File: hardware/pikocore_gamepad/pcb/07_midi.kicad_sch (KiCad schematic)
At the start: 10 parts, among them J6 MIDI IN, J7 MIDI OUT, U10 H11L1M, U9 74LVC1G17

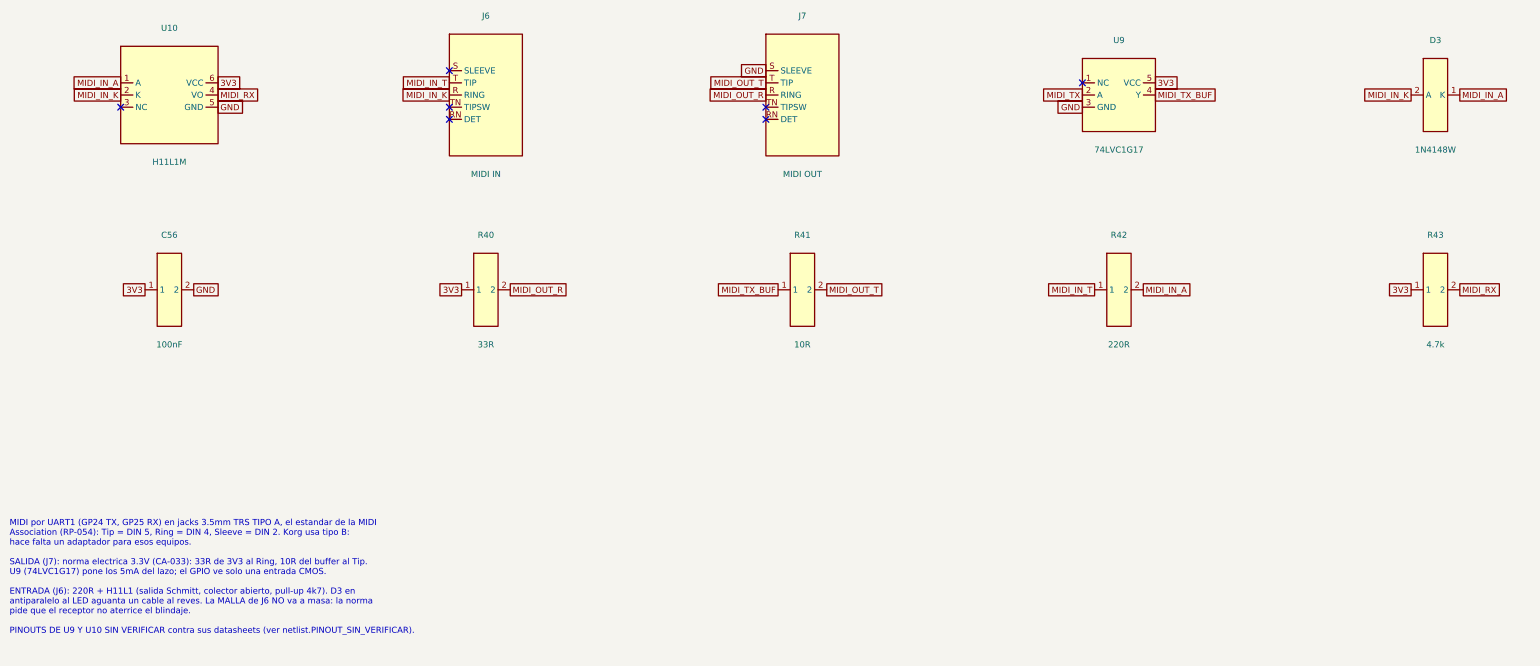
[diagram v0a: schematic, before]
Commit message: hw: pase de correcciones de la revision final (MIDI IN, pines del firmware, nucleo)
- MIDI IN tenia Tip y Ring al reves respecto de la norma: el emisor pone
  corriente por DIN 4 (= Ring en tipo A); ahora Ring -> 220R -> anodo del
  H11L1 y Tip -> catodo. Solo hubiera recibido de equipos tipo B.
- El firmware PIKO_GAMEPAD usaba GP25 (ahora MIDI_RX) como LED y GP27
  (VBUS_SENSE) como clock-in: LED y trigger-out quedan en -1 con guardas en
  main.cpp, el clock-in pasa a GP28. Test nuevo que cruza los literales de
  hw_gamepi13.h contra pinmap.py. Compila.
- Una sola caja medida del nucleo (NUCLEO_BOX) para tests y comentarios.
- route_io.py apaga los asserts de wx: ExportSpecctraDSN abria un dialogo
  modal y colgaba el ciclo. Carriles copiados hasta 12.5mm; bajadas manuales
  de LCD_DC y LCD_MOSI a J4 y de PWR_EN al slide; BTN_START sin carril.

Puertas: 210 tests, ERC 0/0, DRC 0 errores / 0 sin conectar / 0 paridad
(15 avisos), G-0 en rojo solo por LCD_FPC_PIN_ORDER.

Co-Authored-By: Claude Fable 5.1 <noreply@anthropic.com>
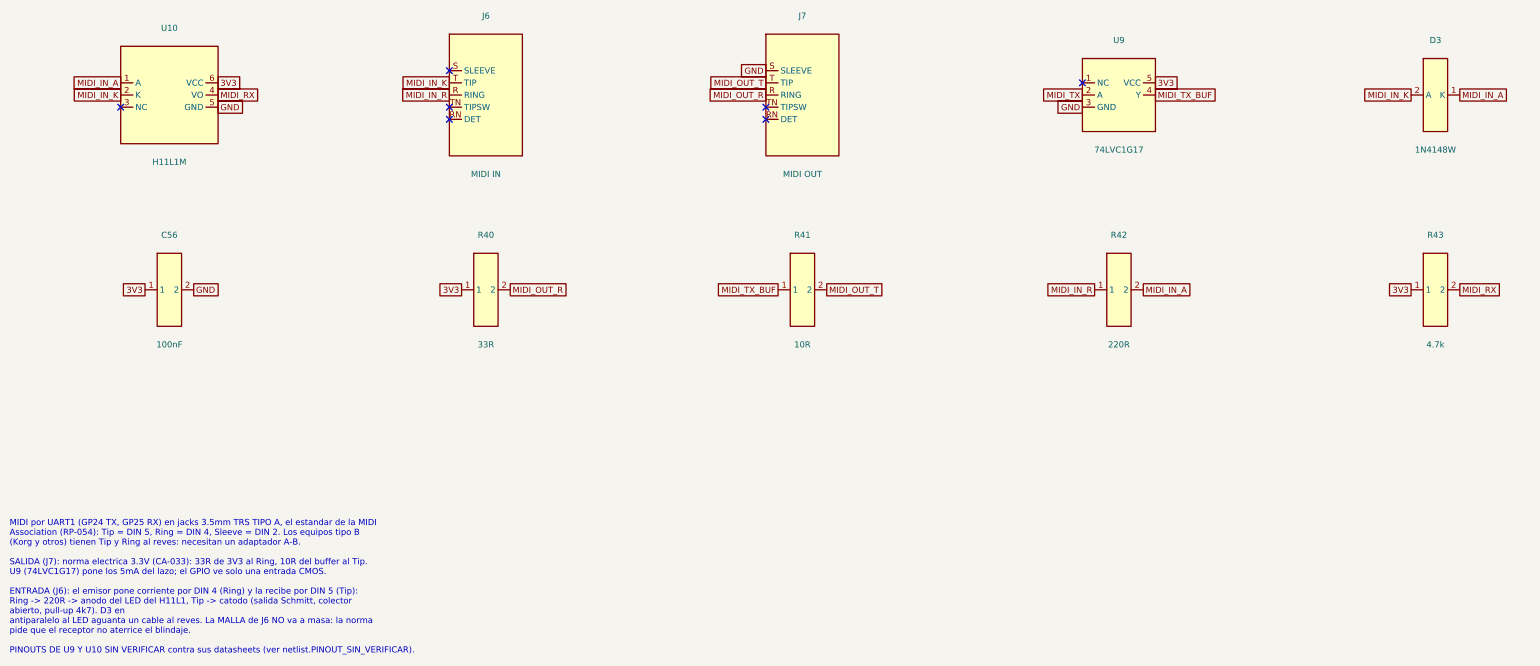
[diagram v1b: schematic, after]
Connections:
- net MIDI_IN_K: now also J6.T (TIP); no longer J6.R (RING)
- net MIDI_IN_T renamed MIDI_IN_R
- net MIDI_IN_R: now also J6.R (RING); no longer J6.T (TIP)
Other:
- note added: "MIDI por UART1 (GP24 TX, GP25 RX) en jacks 3.5mm TRS TIPO A, el estandar de la MIDI Association (RP-054): Tip = DIN 5, Ring = DIN 4, Sleeve = DIN 2. Los equipos tipo B (Korg y otros) tienen Tip y Ring al reves: necesitan un adaptador A-B. SALIDA (J7): norma electrica 3.3V (CA-033): 33R de 3V3 al Ring, 10R del buffer al Tip. U9 (74LVC1G17) pone los 5mA del lazo; el GPIO ve solo una entrada CMOS. E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"
- note removed: "MIDI por UART1 (GP24 TX, GP25 RX) en jacks 3.5mm TRS TIPO A, el estandar de la MIDI Association (RP-054): Tip = DIN 5, Ring = DIN 4, Sleeve = DIN 2. Korg usa tipo B: hace falta un adaptador para esos equipos. SALIDA (J7): norma electrica 3.3V (CA-033): 33R de 3V3 al Ring, 10R del buffer al Tip. U9 (74LVC1G17) pone los 5mA del lazo; el GPIO ve solo una entrada CMOS. ENTRADA (J6): 220R + H11L1 (sal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"
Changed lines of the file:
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@@
   )
   (no_connect (at 111.76 35.56))
-  (global_label "MIDI_IN_T" (shape passive) (at 111.76 38.1 180)
+  (global_label "MIDI_IN_K" (shape passive) (at 111.76 38.1 180)
     (effects (font (size 1.27 1.27)) (justify right))
     (property "Intersheetrefs" "${INTERSHEET_REFS}" (at 111.76 38.1 0) (effects (font (size 1.27 1.27)) (hide yes)))
   )
-  (global_label "MIDI_IN_K" (shape passive) (at 111.76 40.64 180)
+  (global_label "MIDI_IN_R" (shape passive) (at 111.76 40.64 180)
     (effects (font (size 1.27 1.27)) (justify right))
     (property "Intersheetrefs" "${INTERSHEET_REFS}" (at 111.76 40.64 0) (effects (font (size 1.27 1.27)) (hide yes)))
@@
     (property "Intersheetrefs" "${INTERSHEET_REFS}" (at 190.5 81.28 0) (effects (font (size 1.27 1.27)) (hide yes)))
   )
-  (global_label "MIDI_IN_T" (shape passive) (at 246.38 81.28 180)
+  (global_label "MIDI_IN_R" (shape passive) (at 246.38 81.28 180)
     (effects (font (size 1.27 1.27)) (justify right))
     (property "Intersheetrefs" "${INTERSHEET_REFS}" (at 246.38 81.28 0) (effects (font (size 1.27 1.27)) (hide yes)))
@@
     (property "Intersheetrefs" "${INTERSHEET_REFS}" (at 322.58 81.28 0) (effects (font (size 1.27 1.27)) (hide yes)))
   )
-  (text "MIDI por UART1 (GP24 TX, GP25 RX) en jacks 3.5mm TRS TIPO A, el estandar de la MIDI\nAssociation (RP-054): Tip = DIN 5, Ring = DIN 4, Sleeve = DIN 2. Korg usa tipo B:\nhace falta un adaptador para esos equipos.\n\nSALIDA (J7): norma electrica 3.3V (CA-033): 33R de 3V3 al Ring, 10R del buffer al Tip.\nU9 (74LVC1G17) pone los 5mA del lazo; el GPIO ve solo una entrada CMOS.\n\nENTRADA (J6): 220R + H11L1 (salida Schmitt, colector abierto, pull-up 4k7). D3 en\nantiparalelo al LED aguanta un cable al reves. La MALLA de J6 NO va a masa: la norma\npide que el receptor no aterrice el blindaje.\n\nPINOUTS DE U9 Y U10 SIN VERIFICAR contra sus datasheets (ver netlist.PINOUT_SIN_VERIFICAR)." (exclude_from_sim no) (at 20 129.28 0)
+  (text "MIDI por UART1 (GP24 TX, GP25 RX) en jacks 3.5mm TRS TIPO A, el estandar de la MIDI\nAssociation (RP-054): Tip = DIN 5, Ring = DIN 4, Sleeve = DIN 2. Los equipos tipo B\n(Korg y otros) tienen Tip y Ring al reves: necesitan un adaptador A-B.\n\nSALIDA (J7): norma electrica 3.3V (CA-033): 33R de 3V3 al Ring, 10R del buffer al Tip.\nU9 (74LVC1G17) pone los 5mA del lazo; el GPIO ve solo una entrada CMOS.\n\nENTRADA (J6): el emisor pone corriente por DIN 4 (Ring) y la recibe por DIN 5 (Tip):\nRing -> 220R -> anodo del LED del H11L1, Tip -> catodo (salida Schmitt, colector\nabierto, pull-up 4k7). D3 en\nantiparalelo al LED aguanta un cable al reves. La MALLA de J6 NO va a masa: la norma\npide que el receptor no aterrice el blindaje.\n\nPINOUTS DE U9 Y U10 SIN VERIFICAR contra sus datasheets (ver netlist.PINOUT_SIN_VERIFICAR)." (exclude_from_sim no) (at 20 129.28 0)
     (effects (font (size 1.27 1.27)) (justify left top))
   )
